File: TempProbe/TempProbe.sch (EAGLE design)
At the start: 15 parts, among them J1 AVR_SPI_PRG_6PTH, U2 ATTINY841

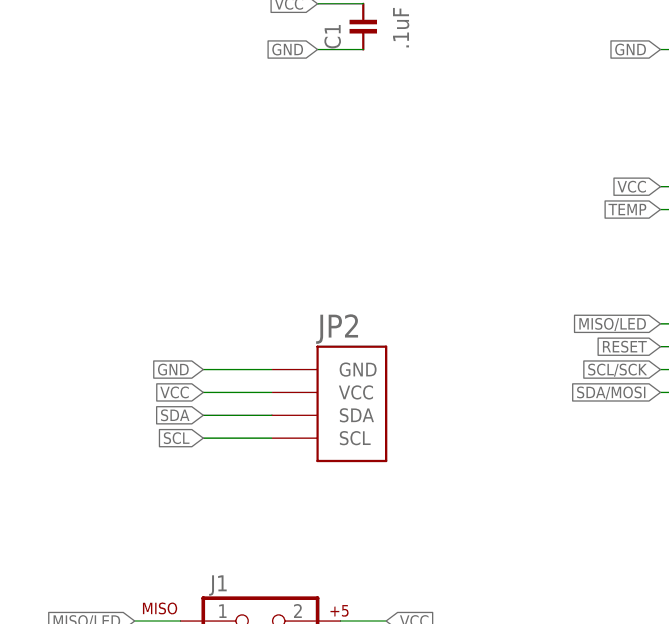
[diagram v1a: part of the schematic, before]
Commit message: Changed to use direct wire soldering for modulo bus instead of a connector.
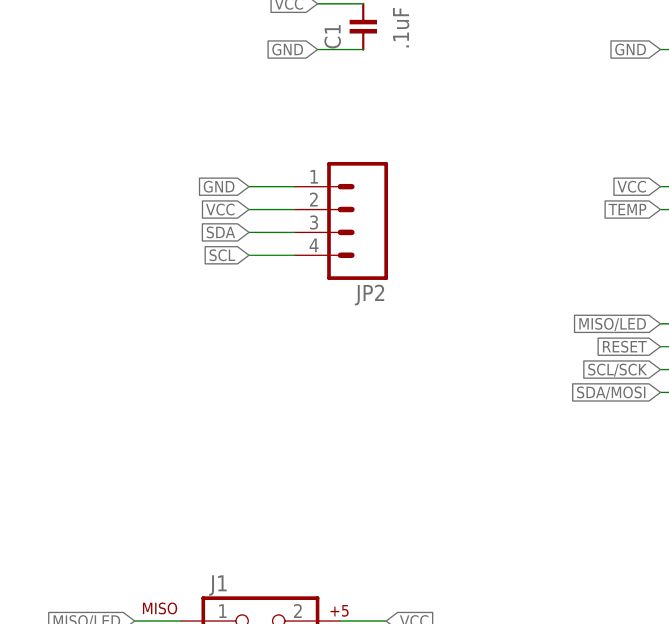
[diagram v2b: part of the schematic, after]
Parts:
- JP2: value HEADER-MODULO -> (none); device Modulo:HEADER-MODULO -> SparkFun-Connectors:M041X04_NO_SILK; BOM (none) -> EXCLUDE
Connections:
- net GND: now also JP2.1; no longer JP2.GND
- net SCL: now also JP2.4; no longer JP2.SCL
- net SDA: now also JP2.3; no longer JP2.SDA
- net VCC: now also JP2.2; no longer JP2.VCC
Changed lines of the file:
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@@
 <attribute name="PARTNUM" value="NTCLE413E2103F102L"/>
 </part>
-<part name="JP2" library="Modulo" deviceset="HEADER-MODULO" device=""/>
 <part name="J1" library="SparkFun-Connectors" deviceset="AVR_SPI_PRG_6" device="PTH"/>
+<part name="JP2" library="SparkFun-Connectors" deviceset="M04" device="1X04_NO_SILK">
+<attribute name="BOM" value="EXCLUDE"/>
+</part>
 </parts>
 <sheets>
@@
 <attribute name="PARTNUM" x="88.9" y="73.66" size="1.778" layer="96" rot="R180" display="off"/>
 </instance>
-<instance part="JP2" gate="G$1" x="45.72" y="101.6"/>
 <instance part="J1" gate="G$1" x="35.56" y="76.2"/>
+<instance part="JP2" gate="G$1" x="45.72" y="124.46" rot="R180">
+<attribute name="BOM" x="45.72" y="124.46" size="1.27" layer="96" rot="R180" display="off"/>
+</instance>
 </instances>
 <busses>
@@
 </segment>
 <segment>
-<pinref part="JP2" gate="G$1" pin="GND"/>
-<wire x1="38.1" y1="106.68" x2="30.48" y2="106.68" width="0.1524" layer="91"/>
-<label x="30.48" y="106.68" size="1.27" layer="95" rot="R180" xref="yes"/>
-</segment>
-<segment>
 <pinref part="J1" gate="G$1" pin="6"/>
 <wire x1="45.72" y1="73.66" x2="50.8" y2="73.66" width="0.1524" layer="91"/>
 <label x="50.8" y="73.66" size="1.27" layer="95" xref="yes"/>
+</segment>
+<segment>
+<pinref part="JP2" gate="G$1" pin="1"/>
+<wire x1="40.64" y1="127" x2="35.56" y2="127" width="0.1524" layer="91"/>
+<label x="35.56" y="127" size="1.27" layer="95" rot="R180" xref="yes"/>
 </segment>
 </net>
@@
 </segment>
 <segment>
-<pinref part="JP2" gate="G$1" pin="SDA"/>
-<wire x1="38.1" y1="101.6" x2="30.48" y2="101.6" width="0.1524" layer="91"/>
-<label x="30.48" y="101.6" size="1.27" layer="95" rot="R180" xref="yes"/>
+<pinref part="JP2" gate="G$1" pin="3"/>
+<wire x1="40.64" y1="121.92" x2="35.56" y2="121.92" width="0.1524" layer="91"/>
+<label x="35.56" y="121.92" size="1.27" layer="95" rot="R180" xref="yes"/>
 </segment>
 </net>
@@
 </segment>
 <segment>
-<pinref part="JP2" gate="G$1" pin="VCC"/>
-<wire x1="38.1" y1="104.14" x2="30.48" y2="104.14" width="0.1524" layer="91"/>
-<label x="30.48" y="104.14" size="1.27" layer="95" rot="R180" xref="yes"/>
-</segment>
-<segment>
 <pinref part="J1" gate="G$1" pin="2"/>
 <wire x1="45.72" y1="78.74" x2="50.8" y2="78.74" width="0.1524" layer="91"/>
 <label x="50.8" y="78.74" size="1.27" layer="95" xref="yes"/>
+</segment>
+<segment>
+<pinref part="JP2" gate="G$1" pin="2"/>
+<wire x1="40.64" y1="124.46" x2="35.56" y2="124.46" width="0.1524" layer="91"/>
+<label x="35.56" y="124.46" size="1.27" layer="95" rot="R180" xref="yes"/>
 </segment>
 </net>
@@
 </segment>
 <segment>
-<pinref part="JP2" gate="G$1" pin="SCL"/>
-<wire x1="38.1" y1="99.06" x2="30.48" y2="99.06" width="0.1524" layer="91"/>
-<label x="30.48" y="99.06" size="1.27" layer="95" rot="R180" xref="yes"/>
+<pinref part="JP2" gate="G$1" pin="4"/>
+<wire x1="40.64" y1="119.38" x2="35.56" y2="119.38" width="0.1524" layer="91"/>
+<label x="35.56" y="119.38" size="1.27" layer="95" rot="R180" xref="yes"/>
 </segment>
 </net>

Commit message: Various changes
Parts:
- J1: BOM (none) -> EXCLUDE
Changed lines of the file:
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@@
 <attribute name="PARTNUM" value="NTCLE413E2103F102L"/>
 </part>
-<part name="J1" library="SparkFun-Connectors" deviceset="AVR_SPI_PRG_6" device="PTH"/>
+<part name="J1" library="SparkFun-Connectors" deviceset="AVR_SPI_PRG_6" device="PTH">
+<attribute name="BOM" value="EXCLUDE"/>
+</part>
 <part name="JP2" library="SparkFun-Connectors" deviceset="M04" device="1X04_NO_SILK">
 <attribute name="BOM" value="EXCLUDE"/>
@@
 <attribute name="PARTNUM" x="88.9" y="73.66" size="1.778" layer="96" rot="R180" display="off"/>
 </instance>
-<instance part="J1" gate="G$1" x="35.56" y="76.2"/>
+<instance part="J1" gate="G$1" x="35.56" y="76.2">
+<attribute name="BOM" x="35.56" y="76.2" size="1.27" layer="96" display="off"/>
+</instance>
 <instance part="JP2" gate="G$1" x="45.72" y="124.46" rot="R180">
 <attribute name="BOM" x="45.72" y="124.46" size="1.27" layer="96" rot="R180" display="off"/>

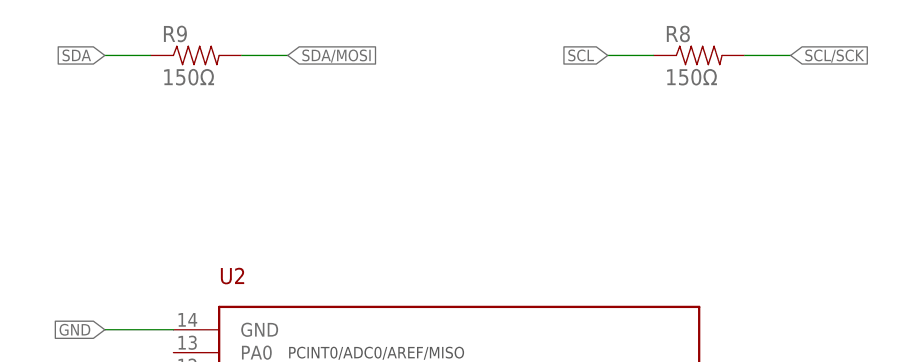
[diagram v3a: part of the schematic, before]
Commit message: Various small tweaks based on testing and feedback from manufacturer.
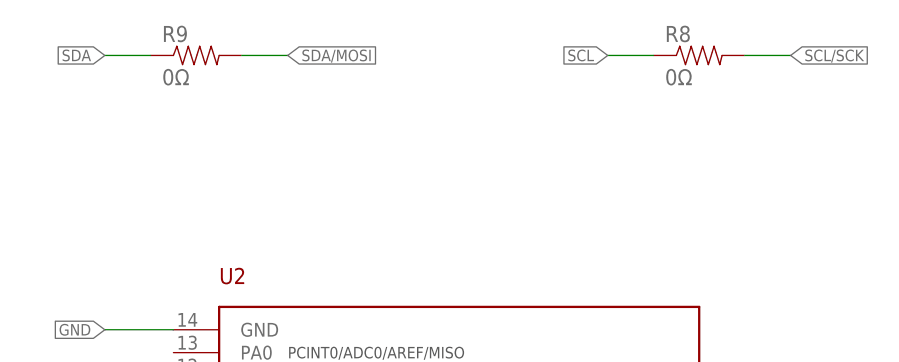
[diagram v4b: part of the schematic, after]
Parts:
- R8, R9: value 150Ω -> 0Ω; device Modulo:RESISTOR-150Ω -> Modulo:RESISTOR-0Ω
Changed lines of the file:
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@@
 </part>
 <part name="U2" library="Modulo" deviceset="ATTINY841" device="" value="ATTINY841"/>
-<part name="R8" library="Modulo" deviceset="RESISTOR" device="-150Ω" value="150Ω">
+<part name="R8" library="Modulo" deviceset="RESISTOR" device="-0Ω" value="0Ω">
 <attribute name="BOM" value="EXCLUDE"/>
 </part>
-<part name="R9" library="Modulo" deviceset="RESISTOR" device="-150Ω" value="150Ω">
+<part name="R9" library="Modulo" deviceset="RESISTOR" device="-0Ω" value="0Ω">
 <attribute name="BOM" value="EXCLUDE"/>
 </part>

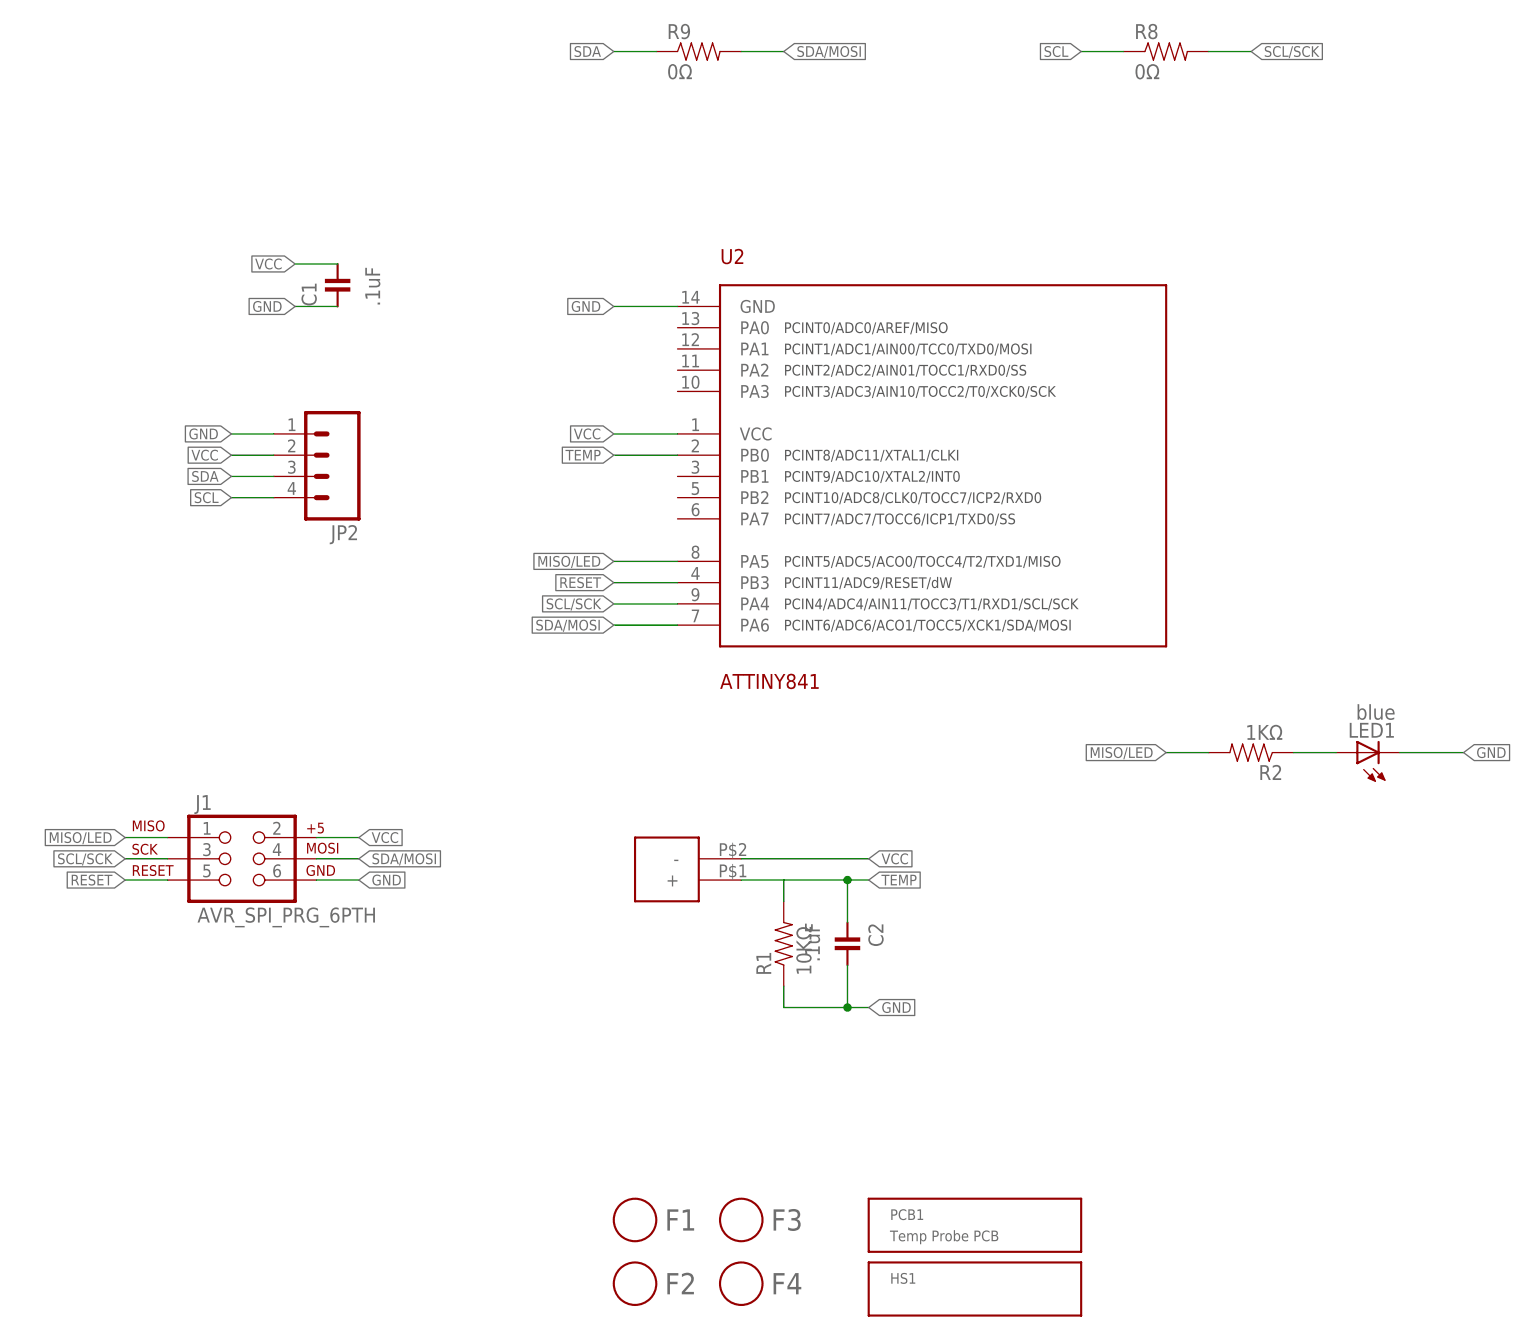
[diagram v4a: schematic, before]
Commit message: Added unique board prefixes to part numbers due to CM requirements
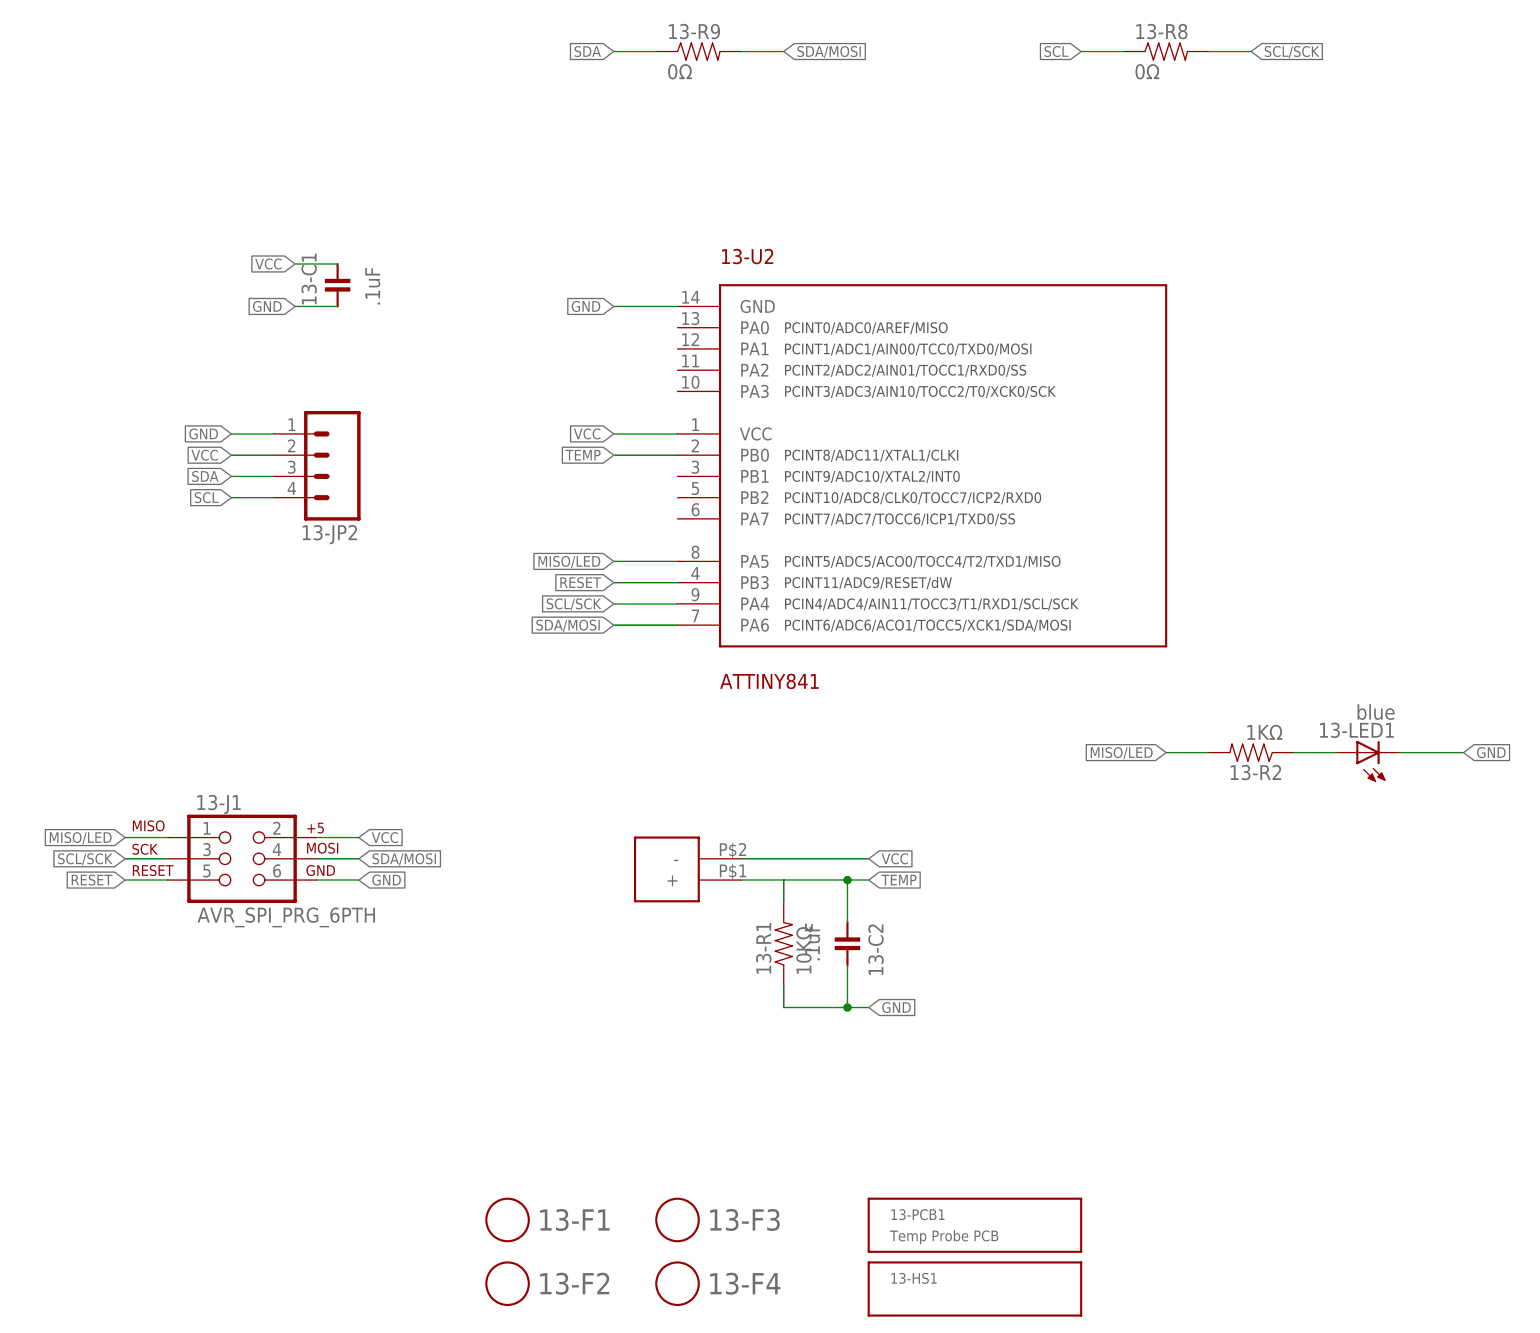
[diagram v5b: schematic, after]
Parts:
- removed F1, F2, F3, F4: FIDUCIAL, Modulo:FIDUCIAL
- added 13-F1, 13-F2, 13-F3, 13-F4: FIDUCIAL, Modulo:FIDUCIAL
- renumbered C1 to 13-C1, C2 to 13-C2, J1 to 13-J1, JP2 to 13-JP2, LED1 to 13-LED1, PROBE1 to 13-PROBE1, R1 to 13-R1, R2 to 13-R2, R8 to 13-R8, R9 to 13-R9, U2 to 13-U2
